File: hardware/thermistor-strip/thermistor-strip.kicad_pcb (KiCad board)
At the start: 2 copper layers, 158 x 12 mm, 0 parts

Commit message: save footprint placement for thermistor strip
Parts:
- added J1: FH19C-7S-0.5SH10, Hirose_FH19C_7S_0_5SH:CONN7_FH19C_7S_HIR, F.Cu at (52.5, 142.0)
- added RT1: NCU18XH103F60RB, Murata_NCU18XH103F60RB:THRMC1608X95N, F.Cu at (204.7, 147.0)
- added RT2: NCU18XH103F60RB, Murata_NCU18XH103F60RB:THRMC1608X95N, F.Cu at (174.9, 147.0)
- added RT3: NCU18XH103F60RB, Murata_NCU18XH103F60RB:THRMC1608X95N, F.Cu at (145.1, 147.0)
- added RT4: NCU18XH103F60RB, Murata_NCU18XH103F60RB:THRMC1608X95N, F.Cu at (115.3, 147.0)
- added RT5: NCU18XH103F60RB, Murata_NCU18XH103F60RB:THRMC1608X95N, F.Cu at (85.5, 147.0)
- added RT6: NCU18XH103F60RB, Murata_NCU18XH103F60RB:THRMC1608X95N, F.Cu at (55.7, 147.0)

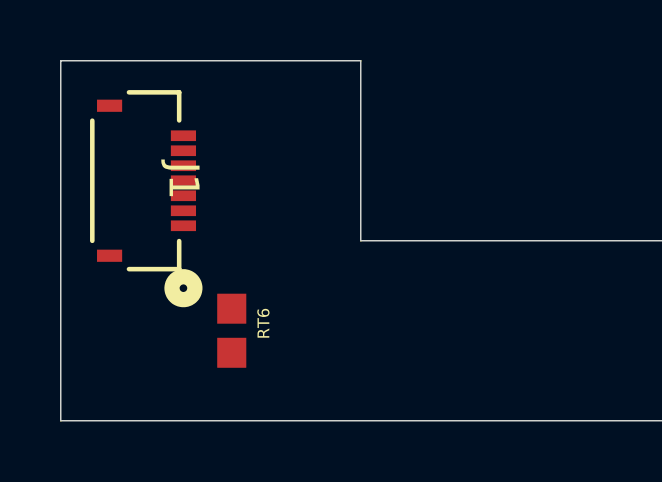
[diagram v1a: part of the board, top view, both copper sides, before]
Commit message: update placement of connector and invert pins for thermistors for more organized traces
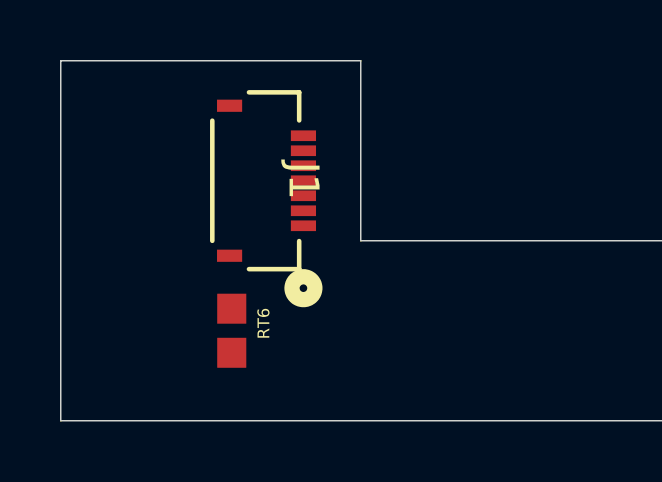
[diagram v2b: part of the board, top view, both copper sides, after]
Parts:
- moved J1 4.00 mm to (56.5, 142.0)
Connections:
- RT1 pad 1: Net-(J1-Pad2) -> Net-(J1-Pad7)
- RT2 pad 1: Net-(J1-Pad3) -> Net-(J1-Pad6)
- RT3 pad 1: Net-(J1-Pad4) -> Net-(J1-Pad5)
- RT4 pad 1: Net-(J1-Pad5) -> Net-(J1-Pad4)
- RT5 pad 1: Net-(J1-Pad6) -> Net-(J1-Pad3)
- RT6 pad 1: Net-(J1-Pad7) -> Net-(J1-Pad2)
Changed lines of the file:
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@@
 			(size 1 0.97)
 			(layers "F.Cu" "F.Mask" "F.Paste")
-			(net "Net-(J1-Pad2)")
+			(net "Net-(J1-Pad7)")
 			(pintype "passive")
 			(solder_mask_margin 0.102)
@@
 			(size 1 0.97)
 			(layers "F.Cu" "F.Mask" "F.Paste")
-			(net "Net-(J1-Pad3)")
+			(net "Net-(J1-Pad6)")
 			(pintype "passive")
 			(solder_mask_margin 0.102)
@@
 			(size 1 0.97)
 			(layers "F.Cu" "F.Mask" "F.Paste")
-			(net "Net-(J1-Pad4)")
+			(net "Net-(J1-Pad5)")
 			(pintype "passive")
 			(solder_mask_margin 0.102)
@@
 			(size 1 0.97)
 			(layers "F.Cu" "F.Mask" "F.Paste")
-			(net "Net-(J1-Pad5)")
+			(net "Net-(J1-Pad4)")
 			(pintype "passive")
 			(solder_mask_margin 0.102)
@@
 			(size 1 0.97)
 			(layers "F.Cu" "F.Mask" "F.Paste")
-			(net "Net-(J1-Pad6)")
+			(net "Net-(J1-Pad3)")
 			(pintype "passive")
 			(solder_mask_margin 0.102)
@@
 			(size 1 0.97)
 			(layers "F.Cu" "F.Mask" "F.Paste")
-			(net "Net-(J1-Pad7)")
+			(net "Net-(J1-Pad2)")
 			(pintype "passive")
 			(solder_mask_margin 0.102)
@@
 	(footprint "Hirose_FH19C_7S_0_5SH:CONN7_FH19C_7S_HIR"
 		(layer "F.Cu")
-		(at 52.5 142 -90)
+		(at 56.5 142 -90)
 		(tags "FH19C-7S-0.5SH10 ")
 		(property "Reference" "J1"

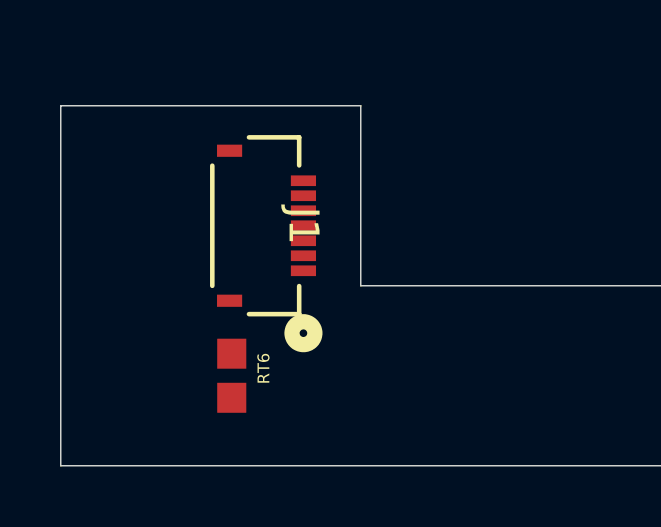
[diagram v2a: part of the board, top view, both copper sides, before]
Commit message: update edge cuts and add clearance for ribbon connector
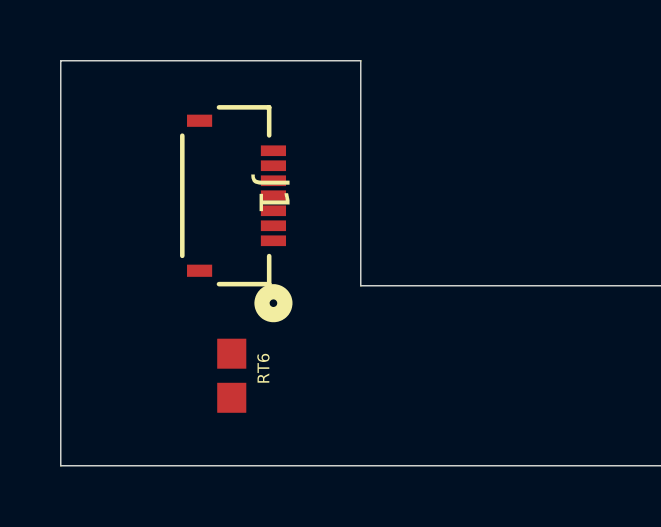
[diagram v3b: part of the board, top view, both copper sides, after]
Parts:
- moved J1 1.41 mm to (55.5, 141.0)
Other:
- board size 158 x 12 mm -> 158 x 13.5 mm
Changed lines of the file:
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@@
 	(footprint "Hirose_FH19C_7S_0_5SH:CONN7_FH19C_7S_HIR"
 		(layer "F.Cu")
-		(at 56.5 142 -90)
+		(at 55.5 141 -90)
 		(tags "FH19C-7S-0.5SH10 ")
 		(property "Reference" "J1"
@@
 	)
 	(gr_line
-		(start 50 138)
+		(start 50 136.5)
 		(end 50 150)
 		(stroke
@@
 			(type solid)
 		)
-		(locked yes)
 		(layer "Edge.Cuts")
 	)
@@
 	)
 	(gr_line
-		(start 60 138)
-		(end 50 138)
+		(start 60 136.5)
+		(end 50 136.5)
 		(stroke
 			(width 0.05)
@@
 	(gr_line
 		(start 60 144)
-		(end 60 138)
+		(end 60 136.5)
 		(stroke
 			(width 0.05)

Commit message: initial tracing progress
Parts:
- moved RT1 1.00 mm to (204.7, 148.0), turned to 0 degrees
- moved RT2 1.00 mm to (174.9, 148.0), turned to 0 degrees
- moved RT3 1.00 mm to (145.1, 148.0), turned to 0 degrees
- moved RT4 1.00 mm to (115.3, 148.0), turned to 0 degrees
- moved RT5 1.00 mm to (85.5, 148.0), turned to 0 degrees
- moved RT6 1.00 mm to (55.7, 148.0), turned to 0 degrees
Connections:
- J1 pad 1: GND -> Net-(J1-Pad1)
- J1 pad 7: Net-(J1-Pad7) -> GND
- RT1 pad 1: Net-(J1-Pad7) -> Net-(J1-Pad1)
- RT2 pad 1: Net-(J1-Pad6) -> Net-(J1-Pad2)
- RT3 pad 1: Net-(J1-Pad5) -> Net-(J1-Pad3)
- RT5 pad 1: Net-(J1-Pad3) -> Net-(J1-Pad5)
- RT6 pad 1: Net-(J1-Pad2) -> Net-(J1-Pad6)
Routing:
- net GND: track 0.00 -> 170.7 mm
- net Net-(J1-Pad1): track 0.00 -> 149.8 mm
- net Net-(J1-Pad2): track 0.00 -> 128.4 mm
- net Net-(J1-Pad3): track 0.00 -> 99.7 mm
- net Net-(J1-Pad4): track 0.00 -> 71.4 mm
- net Net-(J1-Pad5): track 0.00 -> 42.0 mm
- net Net-(J1-Pad6): track 0.00 -> 13.5 mm

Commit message: intial tracing
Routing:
- net GND: track 170.7 -> 172.7 mm
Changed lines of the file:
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@@
+	)
+	(segment
+		(start 175.635 148)
+		(end 175.635 149)
+		(width 0.2)
+		(layer "F.Cu")
+		(net "GND")
+	)
+	(segment
+		(start 145.835 148)
+		(end 145.835 149)
+		(width 0.2)
+		(layer "F.Cu")
+		(net "GND")
 	)
 	(segment
